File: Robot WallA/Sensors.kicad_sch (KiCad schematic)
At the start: 3 parts, among them J32 BM04B-GHS-TBT_LF__SN_, J33 Conn_01x03, J34 BM03B-SRSS-TB

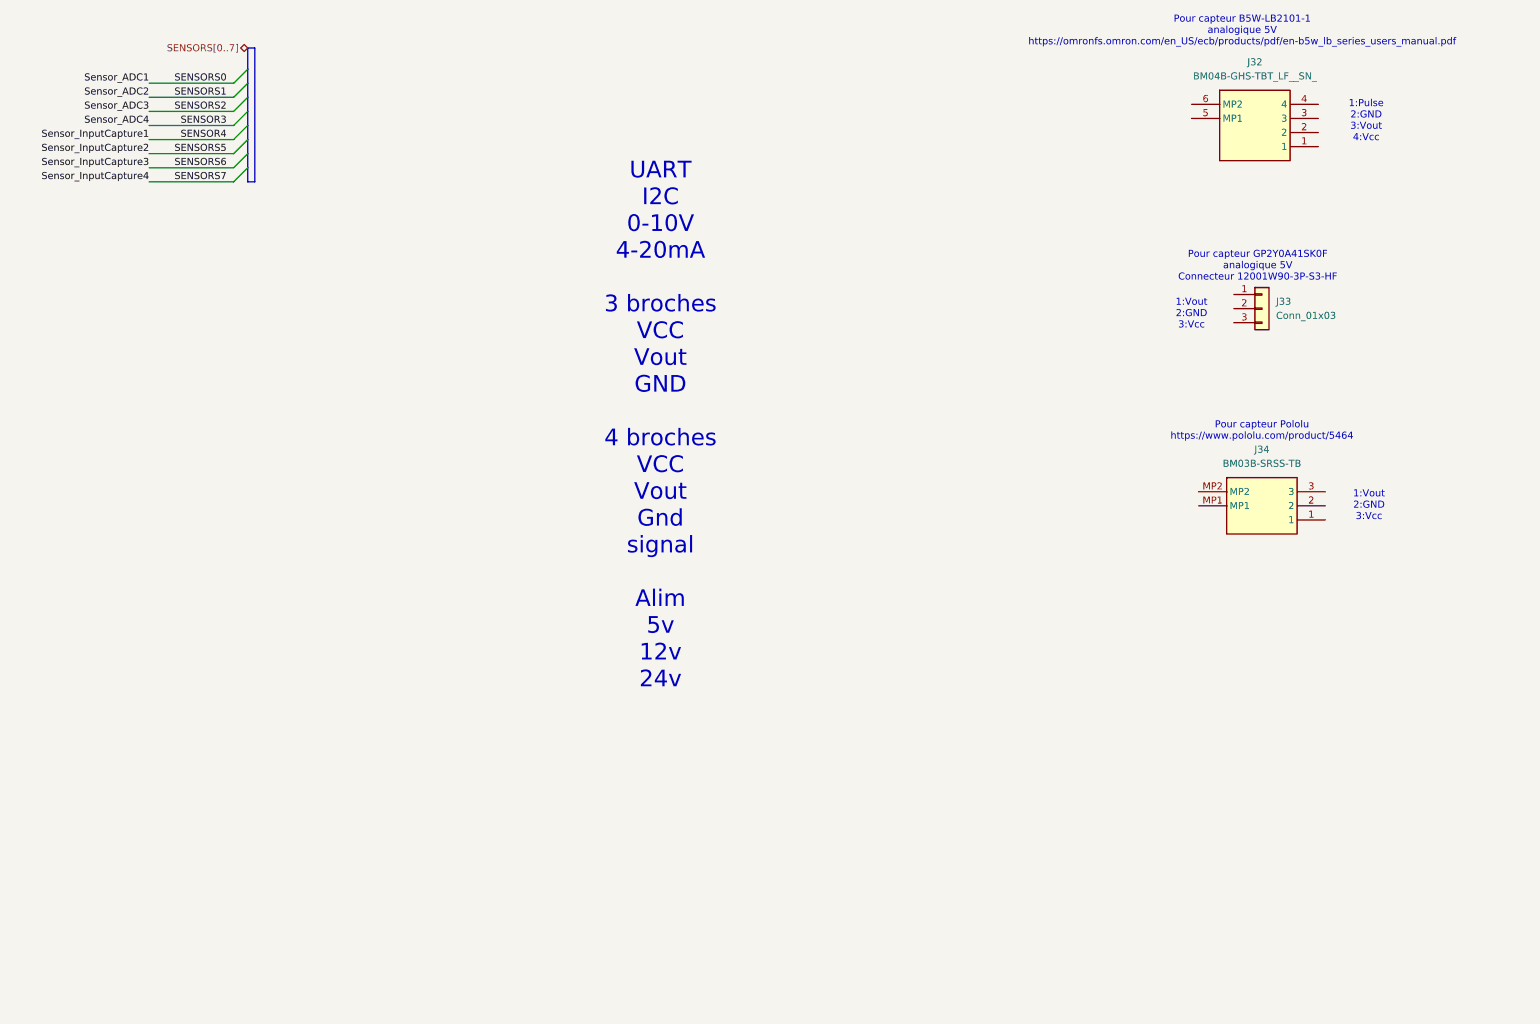
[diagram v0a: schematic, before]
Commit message: Updated USB UART converter, Linked telemeter sensors.
Updated components indicators
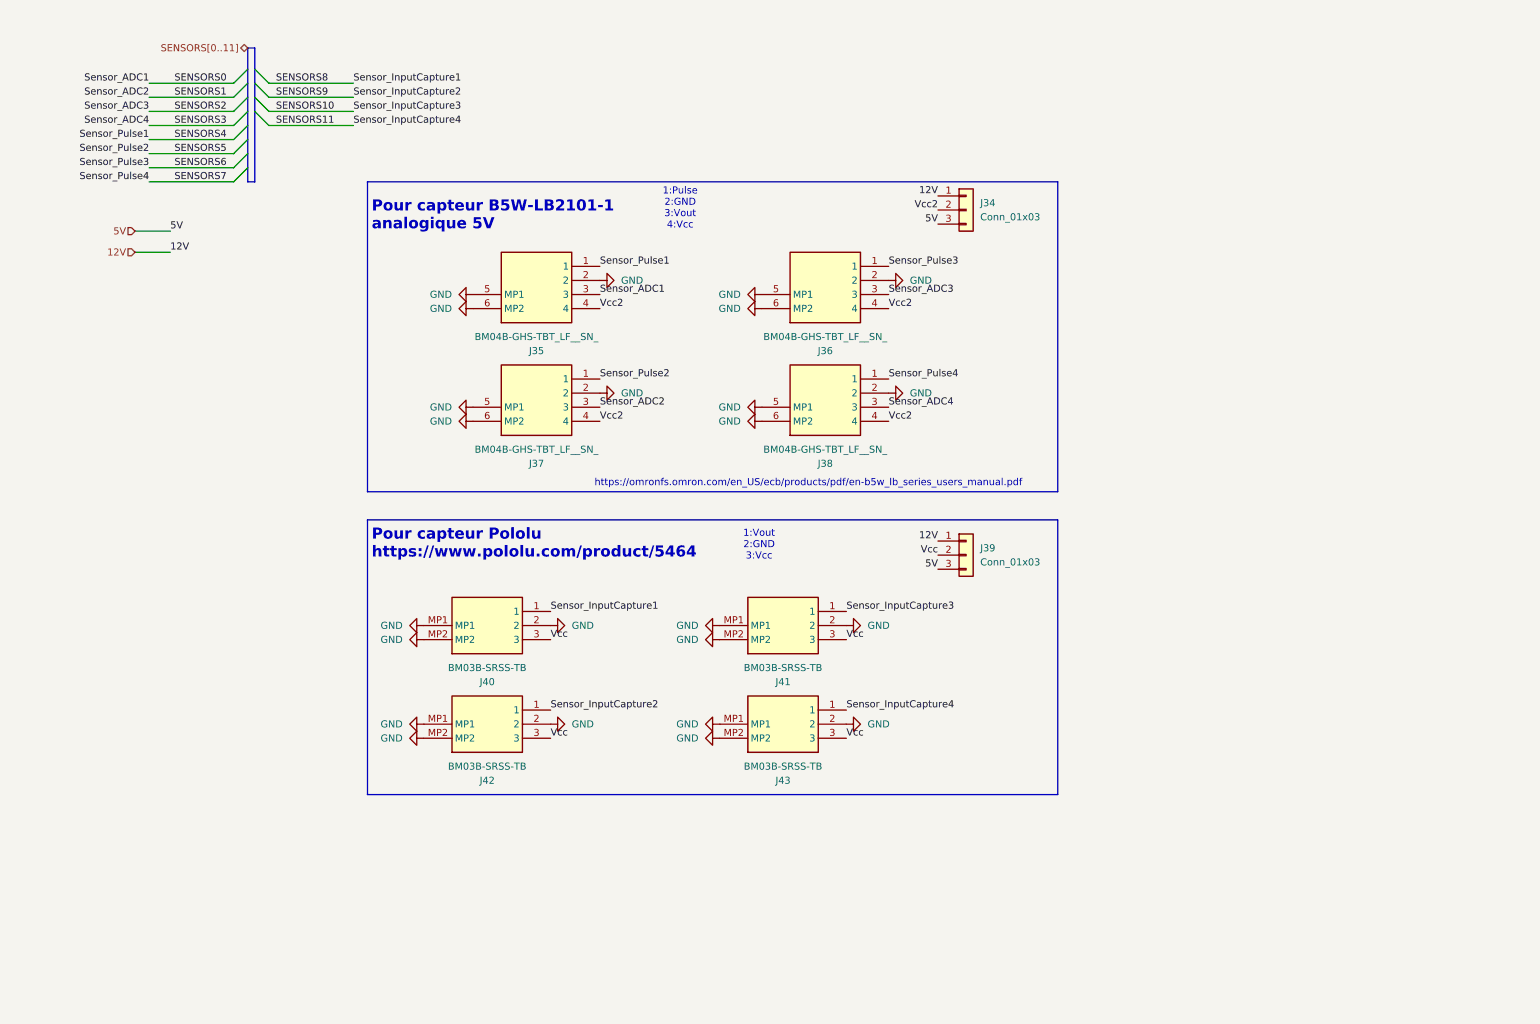
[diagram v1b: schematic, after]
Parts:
- removed J33: Conn_01x03, Connector_PinHeader_2.00mm:PinHeader_1x03_P2.00mm_Vertical, symbol Connector_Generic:Conn_01x03
- added J34, J39: Conn_01x03, Connector_PinHeader_2.54mm:PinHeader_1x03_P2.54mm_Vertical, symbol Connector_Generic:Conn_01x03
- added J36, J37, J38: BM04B-GHS-TBT_LF__SN_, SamacSys_Parts:BM04BGHSTBTLFSN, symbol SamacSys_new:BM04B-GHS-TBT_LF__SN_
- added J40, J41, J43: BM03B-SRSS-TB, SamacSys_Parts:BM03BSRSSTB, symbol SamacSys_new:BM03B-SRSS-TB
- J35: renamed from J32; footprint BM04BGHSTBTLFSN -> SamacSys_Parts:BM04BGHSTBTLFSN
- J42: renamed from J34; footprint BM03BSRSSTB -> SamacSys_Parts:BM03BSRSSTB
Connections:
- net SENSORS0: now also J35.3
- net SENSORS1: now also J37.3
- net SENSORS2: now also J36.3
- net SENSORS5: now also J37.1
- net SENSORS6: now also J36.1
- net SENSORS7: now also J38.1
- net SENSORS4: now reaches J35.1
- net GND: now reaches J35.2
- net GND: now also J35.5 (MP1), J35.6 (MP2), J42.2, J42.MP1, J42.MP2, J36.2, J36.5 (MP1), J36.6 (MP2), J37.2, J37.5 (MP1), J37.6 (MP2), J38.2, J38.5 (MP1), J38.6 (MP2), J40.2, J40.MP1, J40.MP2, J41.2, J41.MP1, J41.MP2, J43.2, J43.MP1, J43.MP2
- net Vcc2: now reaches J35.4
- net Vcc2: now also J34.2 (Pin_2), J36.4, J37.4, J38.4
- net SENSORS9: now reaches J42.1
- net Vcc: now reaches J42.3
- net Vcc: now also J39.2 (Pin_2), J40.3, J41.3, J43.3
- new net 12V: J34.1 (Pin_1), J39.1 (Pin_1)
- new net 5V: J34.3 (Pin_3), J39.3 (Pin_3)
- new net SENSORS10: J41.1
- new net SENSORS11: J43.1
- new net SENSORS3: J38.3
- new net SENSORS8: J40.1
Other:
- note added: "Pour capteur B5W-LB2101-1 analogique 5V"
- note added: "https://omronfs.omron.com/en_US/ecb/products/pdf/en-b5w_lb_series_users_manual.pdf"
- note removed: "Pour capteur B5W-LB2101-1 analogique 5V https://omronfs.omron.com/en_US/ecb/products/pdf/en-b5w_lb_series_users_manual.pdf"
- note removed: "Pour capteur GP2Y0A41SK0F analogique 5V Connecteur 12001W90-3P-S3-HF"
- note removed: "UART I2C 0-10V 4-20mA 3 broches VCC Vout GND 4 broches VCC Vout Gnd signal Alim 5v 12v 24v"
- moved on the sheet: J35, J42

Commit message: Added standard switchs, debug leds and 12V and 5V connectors
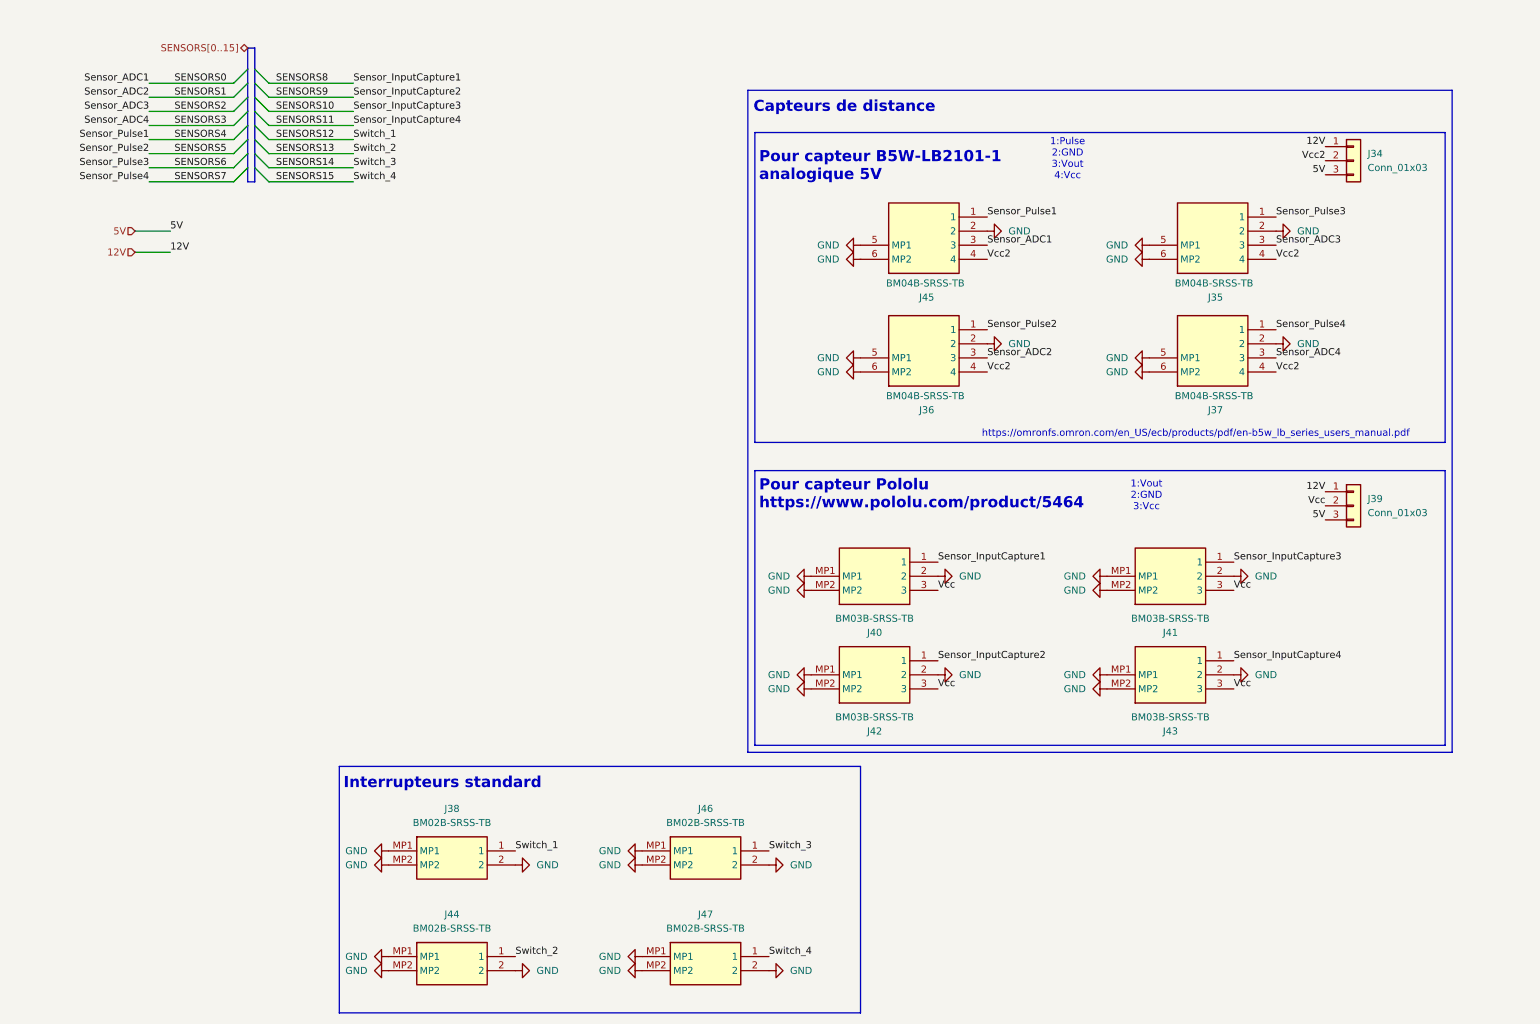
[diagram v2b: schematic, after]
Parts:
- removed J38: BM04B-GHS-TBT_LF__SN_, SamacSys_Parts:BM04BGHSTBTLFSN, symbol SamacSys_new:BM04B-GHS-TBT_LF__SN_
- added J38, J44, J46, J47: BM02B-SRSS-TB, BM02BSRSSTBLFSN, symbol SamacSys_new:BM02B-SRSS-TB_LF__SN_
- added J45: BM04B-SRSS-TB, SamacSys_Parts:BM04B-SRSS-TB_LFSN_, symbol SamacSys_new:BM04B-GHS-TBT_LF__SN_
- J35, J36, J37: value BM04B-GHS-TBT_LF__SN_ -> BM04B-SRSS-TB; footprint SamacSys_Parts:BM04BGHSTBTLFSN -> SamacSys_Parts:BM04B-SRSS-TB_LFSN_; Height 4.2 -> (none); Manufacturer_Name JST (JAPAN SOLDERLESS TERMINALS) -> (none); Manufacturer_Part_Number BM04B-GHS-TBT(LF)(SN) -> BM04B-SRSS-TB; Mouser Part Number 306-BM04BGHSTBTLFSNN -> (none); Mouser Price/Stock https://www.mouser.co.uk/ProductDetail/JST-Commercial/BM04B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 -> (none)
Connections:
- net GND: now also J38.2, J38.MP1, J38.MP2, J44.2, J44.MP1, J44.MP2, J45.2, J45.5 (MP1), J45.6 (MP2), J46.2, J46.MP1, J46.MP2, J47.2, J47.MP1, J47.MP2
- net SENSORS0: now also J45.3; no longer J35.3
- net SENSORS1: now also J36.3; no longer J37.3
- net SENSORS2: now also J35.3; no longer J36.3
- net SENSORS3: now also J37.3
- net SENSORS4: now also J45.1; no longer J35.1
- net SENSORS5: now also J36.1; no longer J37.1
- net SENSORS6: now also J35.1; no longer J36.1
- net SENSORS7: now also J37.1
- net Vcc2: now also J45.4
- new net SENSORS12: J38.1
- new net SENSORS13: J44.1
- new net SENSORS14: J46.1
- new net SENSORS15: J47.1
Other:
- note added: "Capteurs de distance"
- note added: "Interrupteurs standard"
- moved on the sheet: J34, J39, J40, J41, J42, J43

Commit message: Conitnue routing
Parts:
- J38, J44, J46, J47: footprint BM02BSRSSTBLFSN -> SamacSys_Parts:BM02BSRSSTBLFSN
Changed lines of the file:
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@@
 			)
 		)
-		(property "Footprint" "BM02BSRSSTBLFSN"
+		(property "Footprint" "SamacSys_Parts:BM02BSRSSTBLFSN"
 			(at 151.13 279.07 0)
 			(effects
@@
 			)
 		)
-		(property "Footprint" "BM02BSRSSTBLFSN"
+		(property "Footprint" "SamacSys_Parts:BM02BSRSSTBLFSN"
 			(at 151.13 260.02 0)
 			(effects
@@
 			)
 		)
-		(property "Footprint" "BM02BSRSSTBLFSN"
+		(property "Footprint" "SamacSys_Parts:BM02BSRSSTBLFSN"
 			(at 105.41 279.07 0)
 			(effects
@@
 			)
 		)
-		(property "Footprint" "BM02BSRSSTBLFSN"
+		(property "Footprint" "SamacSys_Parts:BM02BSRSSTBLFSN"
 			(at 105.41 260.02 0)
 			(effects

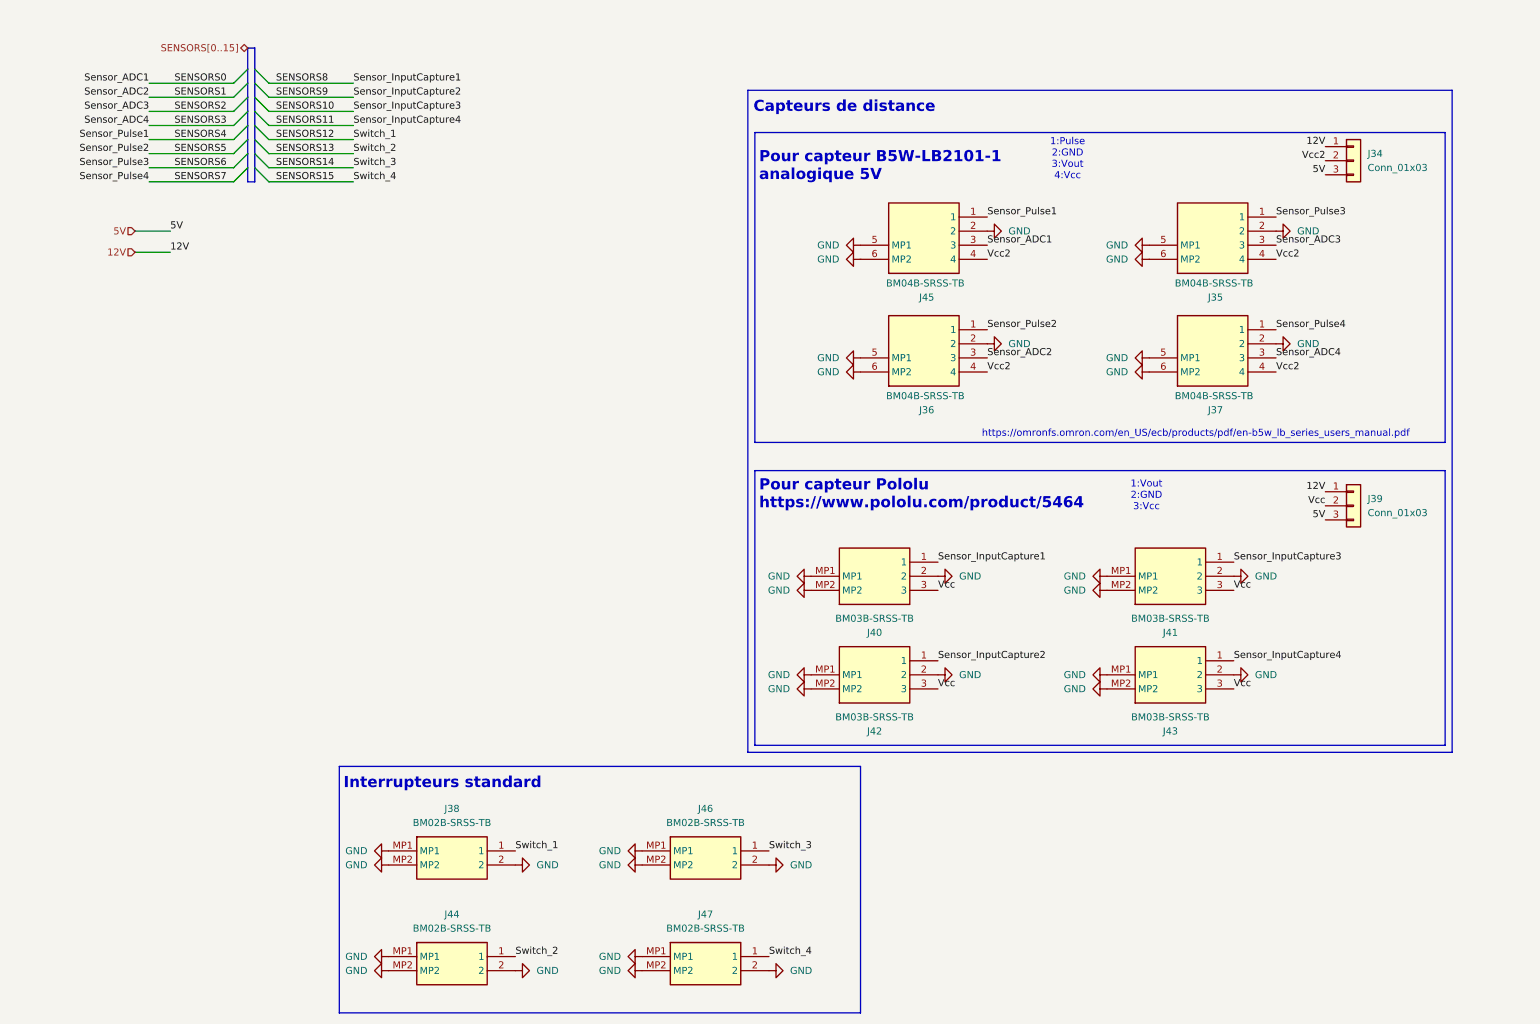
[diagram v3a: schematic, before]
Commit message: Corrected all DRC erros, added info on PCB
modified distance meter connectors to be horizontal
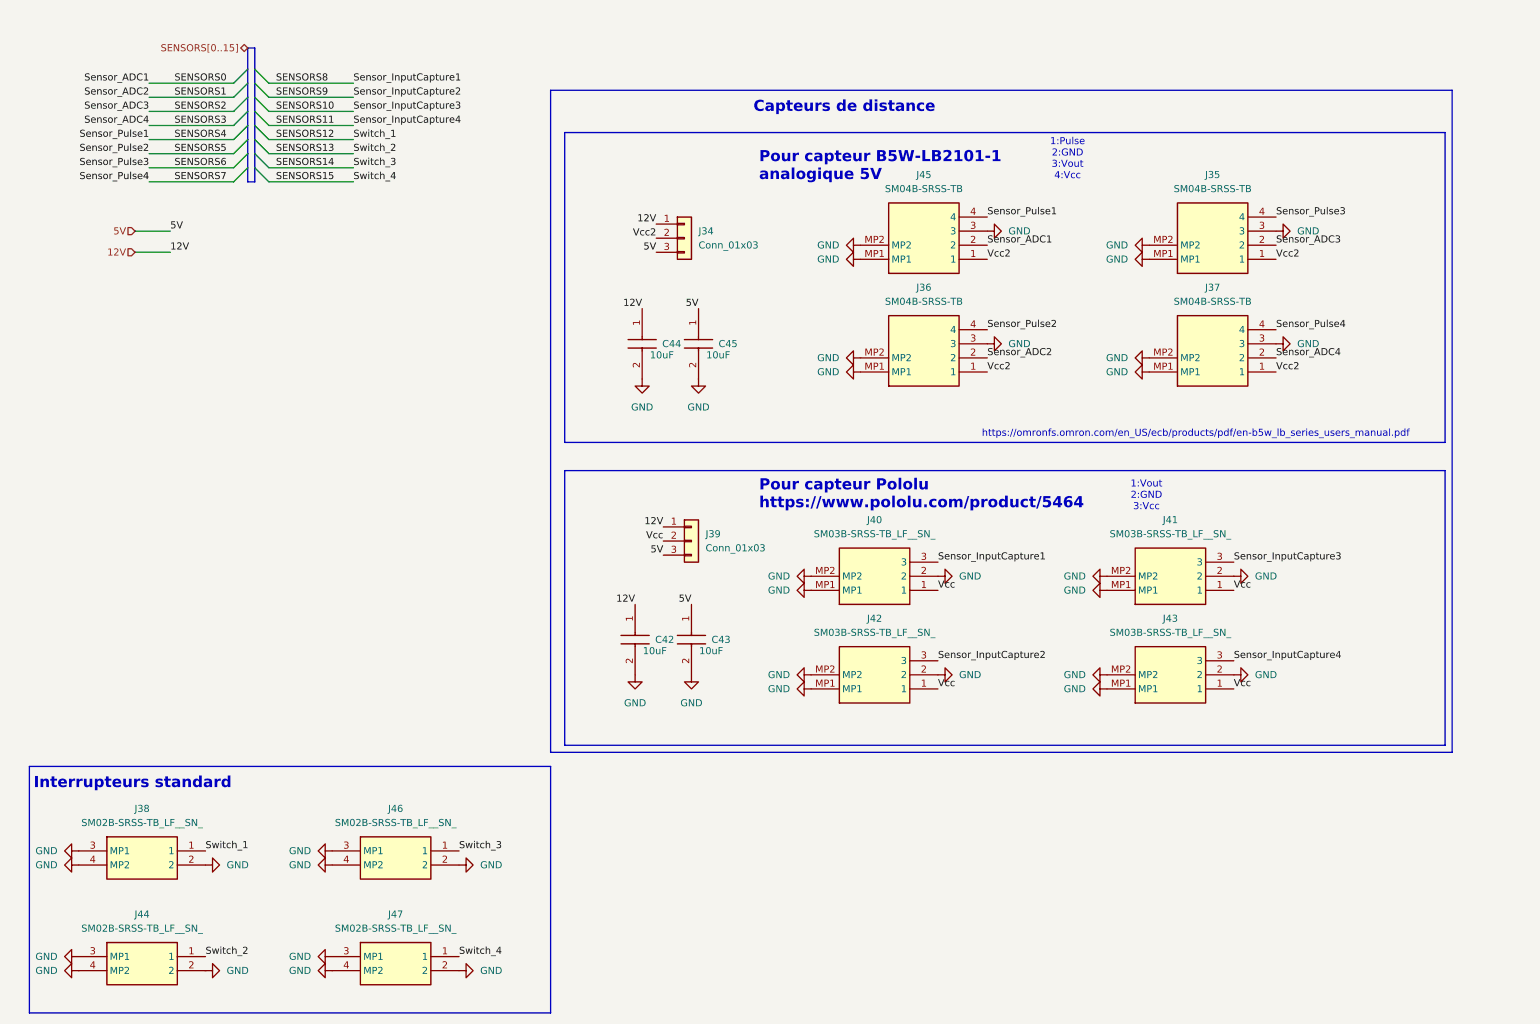
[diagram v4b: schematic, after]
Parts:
- removed J35, J36, J37, J45: BM04B-SRSS-TB, SamacSys_Parts:BM04B-SRSS-TB_LFSN_, symbol SamacSys_new:BM04B-GHS-TBT_LF__SN_
- removed J38, J44, J46, J47: BM02B-SRSS-TB, SamacSys_Parts:BM02BSRSSTBLFSN, symbol SamacSys_new:BM02B-SRSS-TB_LF__SN_
- removed J40, J41, J42, J43: BM03B-SRSS-TB, SamacSys_Parts:BM03BSRSSTB, symbol SamacSys_new:BM03B-SRSS-TB
- added C42, C43, C44, C45: 10uF, Capacitor_SMD:C_0603_1608Metric_Pad1.08x0.95mm_HandSolder, symbol SamacSys_Parts:0805DC104MAT2A
- added J35, J36, J37, J45: SM04B-SRSS-TB, SamacSys_Parts:SM04BSRSSTB, symbol SamacSys_new:SM04B-SRSS-TB
- added J38, J44, J46, J47: SM02B-SRSS-TB_LF__SN_, SM02BSRSSTBLFSN, symbol SamacSys_new:SM02B-SRSS-TB_LF__SN_
- added J40, J41, J42, J43: SM03B-SRSS-TB_LF__SN_, SM03BSRSSTBLFSN, symbol SamacSys_new:SM03B-SRSS-TB_LF__SN_
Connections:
- net 12V: now also C42.1, C44.1
- net 5V: now also C43.1, C45.1
- net GND: now also C42.2, C43.2, C44.2, C45.2, J35.3, J35.MP1, J35.MP2, J36.3, J36.MP1, J36.MP2, J37.3, J37.MP1, J37.MP2, J38.2, J38.3 (MP1), J38.4 (MP2), J40.2, J40.MP1, J40.MP2, J41.2, J41.MP1, J41.MP2, J42.2, J42.MP1, J42.MP2, J43.2, J43.MP1, J43.MP2, J44.2, J44.3 (MP1), J44.4 (MP2), J45.3, J45.MP1, J45.MP2, J46.2, J46.3 (MP1), J46.4 (MP2), J47.2, J47.3 (MP1), J47.4 (MP2)
- net SENSORS0: now also J45.2
- net SENSORS1: now also J36.2
- net SENSORS10: now also J41.3
- net SENSORS11: now also J43.3
- net SENSORS12: now also J38.1
- net SENSORS13: now also J44.1
- net SENSORS14: now also J46.1
- net SENSORS15: now also J47.1
- net SENSORS2: now also J35.2
- net SENSORS3: now also J37.2
- net SENSORS4: now also J45.4
- net SENSORS5: now also J36.4
- net SENSORS6: now also J35.4
- net SENSORS7: now also J37.4
- net SENSORS8: now also J40.3
- net SENSORS9: now also J42.3
- net Vcc: now also J40.1, J41.1, J42.1, J43.1
- net Vcc2: now also J35.1, J36.1, J37.1, J45.1
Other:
- moved on the sheet: J34, J39
